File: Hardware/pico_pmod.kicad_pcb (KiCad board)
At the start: 2 copper layers, 66 x 43.2 mm, 6 parts, among them J1 Conn_02x15_Odd_Even, J2 Conn_01x02, J3 Conn_01x02, J4 Conn_01x02, J5 Conn_01x03, U1 Pico

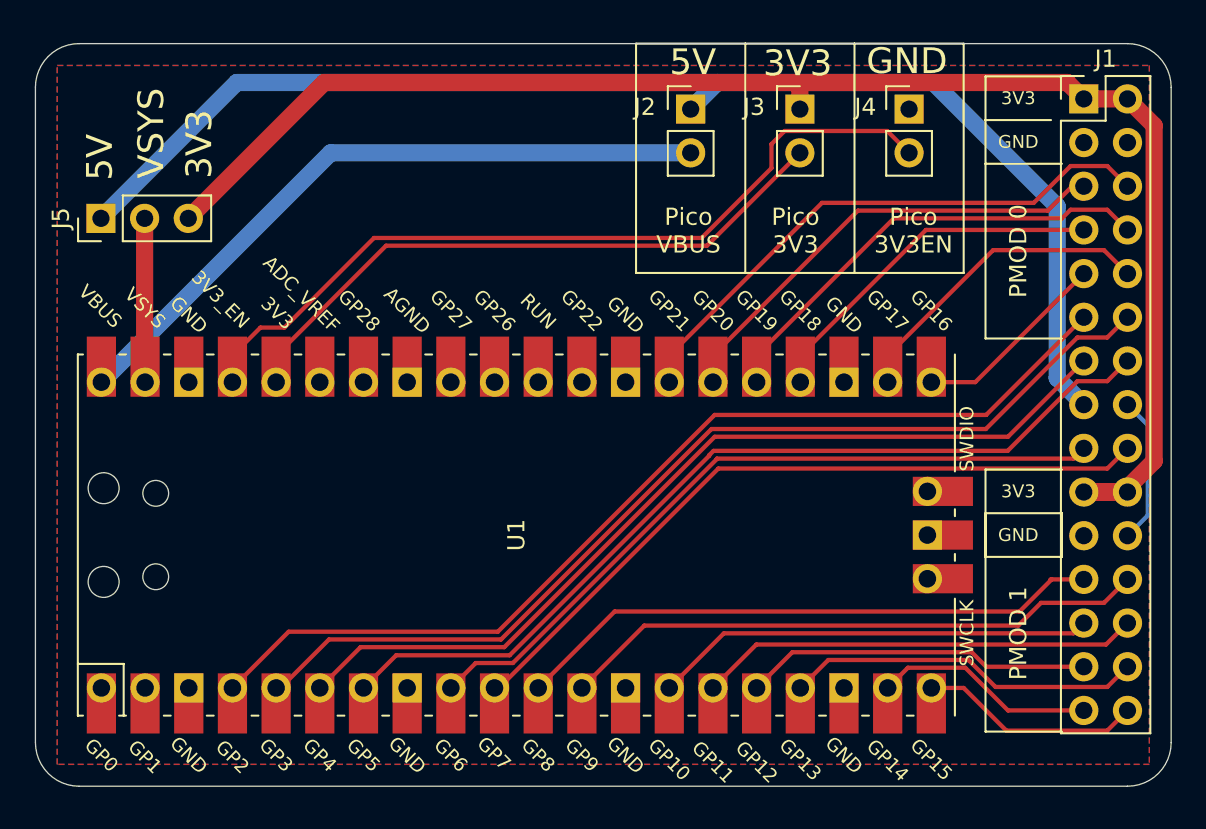
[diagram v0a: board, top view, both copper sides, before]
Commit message: breakout ADC inputs to pins
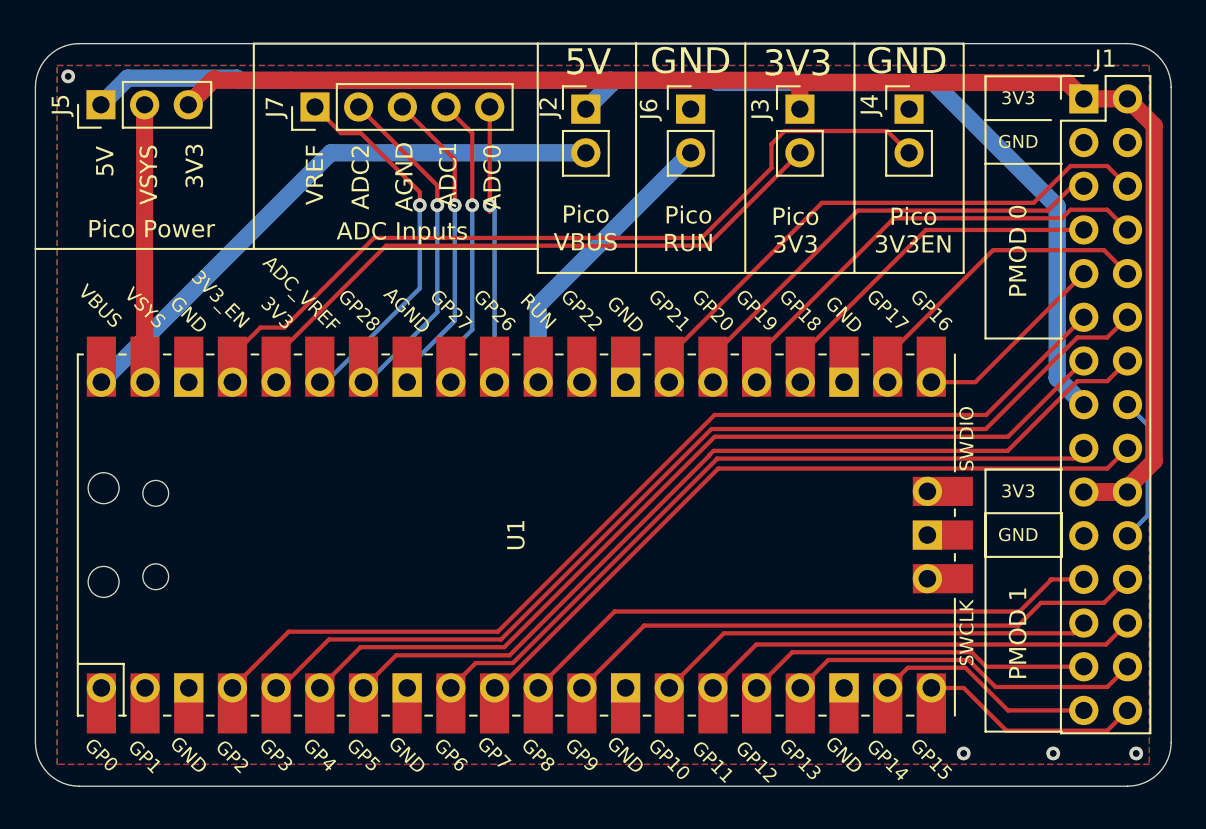
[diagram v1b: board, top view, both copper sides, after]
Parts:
- added J6: Conn_01x02, Connector_PinHeader_2.54mm:PinHeader_1x02_P2.54mm_Vertical, F.Cu at (152.4, 77.5)
- added J7: Conn_01x05, Connector_PinHeader_2.54mm:PinHeader_1x05_P2.54mm_Vertical, F.Cu at (130.6, 77.3)
- moved J5 6.60 mm to (118.1, 77.2)
- moved J2 6.10 mm to (146.3, 77.5)
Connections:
- U1 pad 30: Net-(U1-Pad30) -> Pico_Run
- U1 pad 31: Net-(U1-Pad31) -> ADC0
- U1 pad 32: Net-(U1-Pad32) -> ADC1
- U1 pad 33: Net-(U1-Pad33) -> AGND
- U1 pad 34: Net-(U1-Pad34) -> ADC2
- U1 pad 35: Net-(U1-Pad35) -> ADC_VREF
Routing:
- net ADC_VREF: track 0.00 -> 21.8 mm, vias 0 -> 1
- net ADC2: track 0.00 -> 19.8 mm, vias 0 -> 1
- net AGND: track 0.00 -> 18.4 mm, vias 0 -> 1
- net ADC1: track 0.00 -> 17.4 mm, vias 0 -> 1
- net Pico_Run: track 0.00 -> 17.0 mm
- net ADC0: track 0.00 -> 16.5 mm, vias 0 -> 1
- net Pico_VSYS: track 9.54 -> 16.1 mm
- net Pico_VBUS: track 39.8 -> 33.7 mm
- net +5V: track 76.2 -> 73.9 mm
- net GND: vias 0 -> 4
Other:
- board text added: "ADC Inputs"
- board text added: "ADC0"
- board text added: "ADC1"
- board text added: "ADC2"
- board text added: "AGND"
- board text added: "Pico Power"
- board text added: "Pico RUN"
- board text added: "Raspberry Pico PMod @JamesjHorton JJHorton.co.uk"
- board text added: "VREF"

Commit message: minor silkscreen changes before ordering
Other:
- board text added: "Raspberry Pi Pico PMod @JamesjHorton JJHorton.co.uk"
- board text removed: "Raspberry Pico PMod @JamesjHorton JJHorton.co.uk"
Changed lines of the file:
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@@
       (outputformat 1)
       (mirror false)
-      (drillshape 1)
+      (drillshape 0)
       (scaleselection 1)
       (outputdirectory ""))
@@
     (effects (font (size 1.5 1.5) (thickness 0.3)))
   )
-  (gr_text "Raspberry Pico PMod \n\n@JamesjHorton\nJJHorton.co.uk" (at 146.685 95.25) (layer B.SilkS)
+  (gr_text "Raspberry Pi Pico PMod \n\n@JamesjHorton\nJJHorton.co.uk" (at 144.78 95.25) (layer B.SilkS)
     (effects (font (size 3 3) (thickness 0.45)) (justify mirror))
   )

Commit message: Add Run switch to the PCB
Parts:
- added SW1: SW_Push, Button_Switch_THT:SW_PUSH_6mm_H4.3mm, F.Cu at (116.6, 83.2)
- moved J7 10.8 mm to (141.2, 75.7), turned to 0 degrees
- moved J5 9.02 mm to (125.7, 82.0), turned to 180 degrees
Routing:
- net Pico_Run: track 17.0 -> 58.8 mm, vias 0 -> 1
- net Pico_VBUS: track 33.7 -> 58.8 mm
- net ADC0: track 16.5 -> 7.59 mm, vias 1 -> 0
- net ADC1: track 17.4 -> 11.6 mm, vias 1 -> 0
- net +3V3: track 88.5 -> 83.9 mm
- net +5V: track 73.9 -> 69.7 mm
- net Pico_VSYS: track 16.1 -> 19.9 mm
- net AGND: track 18.4 -> 14.7 mm, vias 1 -> 0
- net ADC2: track 19.8 -> 18.5 mm, vias 1 -> 0
- net GND: track 8.59 -> 9.87 mm, vias 4 -> 3
- net ADC_VREF: track 21.8 -> 22.2 mm, vias 1 -> 0
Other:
- board text added: "Run"

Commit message: Remove Run Header pins
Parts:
- removed J6: Conn_01x02, Connector_PinHeader_2.54mm:PinHeader_1x02_P2.54mm_Vertical
- moved J2 6.22 mm to (152.5, 77.6)
- moved J7 5.02 mm to (136.5, 77.5), turned to 90 degrees
- moved J5 4.62 mm to (126.4, 77.5), turned to 90 degrees
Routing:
- net Pico_Run: track 58.8 -> 39.9 mm
- net ADC0: track 7.59 -> 21.3 mm
- net +3V3: track 83.9 -> 96.7 mm
- net ADC1: track 11.6 -> 19.1 mm
- net Pico_VSYS: track 19.9 -> 23.9 mm
- net AGND: track 14.7 -> 18.2 mm
- net ADC_VREF: track 22.2 -> 19.4 mm
- net Pico_VBUS: track 58.8 -> 56.2 mm
- net +5V: track 69.7 -> 71.1 mm
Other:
- board text removed: "Pico RUN"
